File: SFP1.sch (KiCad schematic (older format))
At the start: 20 parts, among them J3 TYCO_1888247-1

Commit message: mark SFP TX_DIS pulldown resistors as 0 Ohm DNF
R84 R105 R185 R187
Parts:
- R105: value R0402_10K_1%_0.0625W_100PPM -> R0402_0R_JUMPER; symbol Resistors_SMD:R0402_10K_1%_0.0625W_100PPM -> Resistors_SMD:R0402_0R_JUMPER; Comment =Value -> 0; ComponentHeight ~~ -> (none); Database Table Name (none) -> Resistors SMD; Footprint Library (none) -> Resistors SMD; Library Name Resistors SMD -> Resistors.DbLib; Library Ref Resistor - 1% -> Resistor; Manufacturer Part Number R0402_10K_1%_0.0625W_100PPM -> R0402_0R_JUMPER; Manufacturer1 Part Number 232270671003L -> 232270591001L; PackageDescription ~~ -> (none); Part Description General Purpose Thick Film Chip Resistor -> 1A (0.05R Max DC Resistance) Zero Ohm Jumper; Part Number R0402_10K_1%_0.0625W_100PPM -> R0402_0R_JUMPER; Power 0.0625W -> (none); Sense Comment ~~ -> (none); Status Comment ~~ -> (none); TC ±100ppm/°C -> (none); Tolerance ±1% -> (none); Val 10k -> 0; Voltage ~~ -> (none); ~ 10k -> DNP
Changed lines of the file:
@@
 $EndComp
 $Comp
-L Resistors_SMD:R0402_10K_1%_0.0625W_100PPM R?
+L Resistors_SMD:R0402_0R_JUMPER R?
 U 1 1 5C64FA82
 P 7750 3850
@@
 AR Path="/5BABAC65/5C64FA82" Ref="R105"  Part="1"
 F 0 "R105" V 7854 3910 50  0000 L CNN
-F 1 "R0402_10K_1%_0.0625W_100PPM" H 7750 3640 60  0001 L CNN
+F 1 "R0402_0R_JUMPER" H 7750 3640 60  0001 L CNN
 F 2 "Marble:RESC1005X40N" H 7750 2830 60  0001 L CNN
 F 3 "\\\\cern.ch\\dfs\\Applications\\Altium\\Datasheets\\R0402_Phycomp_RC0402.pdf" H 7750 3460 60  0001 L CNN
-F 4 "10k" V 7945 3910 50  0000 L CNN "~"
-F 5 "R0402_10K_1%_0.0625W_100PPM" H 7750 3370 60  0001 L CNN "Part Number"
-F 6 "Resistor - 1%" H 7750 3280 60  0001 L CNN "Library Ref"
+F 4 "DNP" V 7945 3910 50  0000 L CNN "~"
+F 5 "R0402_0R_JUMPER" H 7750 3370 60  0001 L CNN "Part Number"
+F 6 "Resistor" H 7750 3280 60  0001 L CNN "Library Ref"
 F 7 "SchLib\\Resistors.SchLib" H 7750 3190 60  0001 L CNN "Library Path"
-F 8 "=Value" H 7750 3100 60  0001 L CNN "Comment"
+F 8 "0" H 7750 3100 60  0001 L CNN "Comment"
 F 9 "Standard" H 7750 3010 60  0001 L CNN "Component Kind"
 F 10 "Standard" H 7750 2920 60  0001 L CNN "Component Type"
-F 11 "~~" H 7750 2740 60  0001 L CNN "PackageDescription"
+F 11 " " H 7750 2740 60  0001 L CNN "PackageDescription"
 F 12 "2" H 7750 2650 60  0001 L CNN "Pin Count"
 F 13 "PcbLib\\Resistors SMD.PcbLib" H 7750 2560 60  0001 L CNN "Footprint Path"
 F 14 "RESC1005X40N" H 7750 2470 60  0001 L CNN "Footprint Ref"
-F 15 "10k" H 7750 2380 60  0001 L CNN "Val"
+F 15 "0" H 7750 2380 60  0001 L CNN "Val"
 F 16 "Not Recommended" H 7750 2290 60  0001 L CNN "Status"
-F 17 "0.0625W" H 7750 2200 60  0001 L CNN "Power"
-F 18 "±100ppm/°C" H 7750 2110 60  0001 L CNN "TC"
-F 19 "~~" H 7750 2020 60  0001 L CNN "Voltage"
-F 20 "±1%" H 7750 1930 60  0001 L CNN "Tolerance"
-F 21 "General Purpose Thick Film Chip Resistor" H 7750 1840 60  0001 L CNN "Part Description"
+F 17 " " H 7750 2200 60  0001 L CNN "Power"
+F 18 " " H 7750 2110 60  0001 L CNN "TC"
+F 19 " " H 7750 2020 60  0001 L CNN "Voltage"
+F 20 " " H 7750 1930 60  0001 L CNN "Tolerance"
+F 21 "1A (0.05R Max DC Resistance) Zero Ohm Jumper" H 7750 1840 60  0001 L CNN "Part Description"
 F 22 "GENERIC" H 7750 1750 60  0001 L CNN "Manufacturer"
-F 23 "R0402_10K_1%_0.0625W_100PPM" H 7750 1660 60  0001 L CNN "Manufacturer Part Number"
+F 23 "R0402_0R_JUMPER" H 7750 1660 60  0001 L CNN "Manufacturer Part Number"
 F 24 "0402" H 7750 1570 60  0001 L CNN "Case"
 F 25 "No" H 7750 1480 60  0001 L CNN "PressFit"
 F 26 "Yes" H 7750 1390 60  0001 L CNN "Mounted"
-F 27 "~~" H 7750 1300 60  0001 L CNN "Sense Comment"
+F 27 " " H 7750 1300 60  0001 L CNN "Sense Comment"
 F 28 "No" H 7750 1210 60  0001 L CNN "Sense"
-F 29 "~~" H 7750 1120 60  0001 L CNN "Status Comment"
+F 29 " " H 7750 1120 60  0001 L CNN "Status Comment"
 F 30 "No" H 7750 1030 60  0001 L CNN "Socket"
 F 31 "Yes" H 7750 940 60  0001 L CNN "SMD"
-F 32 "~~" H 7750 850 60  0001 L CNN "ComponentHeight"
+F 32 " " H 7750 850 60  0001 L CNN "ComponentHeight"
 F 33 "YAGEO PHYCOMP" H 7750 760 60  0001 L CNN "Manufacturer1 Example"
-F 34 "232270671003L" H 7750 670 60  0001 L CNN "Manufacturer1 Part Number"
+F 34 "232270591001L" H 7750 670 60  0001 L CNN "Manufacturer1 Part Number"
 F 35 "0.4mm" H 7750 580 60  0001 L CNN "Manufacturer1 ComponentHeight"
 F 36 "\\\\cern.ch\\dfs\\Applications\\Altium\\Datasheets\\R0402_Phycomp_RC0402.pdf" H 7750 490 60  0001 L CNN "HelpURL"
@@
 F 38 "12/03/07 00:00:00" H 7750 310 60  0001 L CNN "CreateDate"
 F 39 "10/17/12 00:00:00" H 7750 220 60  0001 L CNN "LatestRevisionDate"
-F 40 "Resistors SMD" H 7750 130 60  0001 L CNN "Library Name"
+F 40 "Resistors.DbLib" H 7750 130 60  0001 L CNN "Library Name"
 F 41 "This work is licensed under the Creative Commons CC-BY-SA 4.0 License. To the extent that circuit schematics that use Licensed Material can be considered to be ‘Adapted Material’, then the copyright holder waives article 3.b of the license with respect to these schematics." H 7750 40  60  0001 L CNN "License"
+F 42 "Resistors SMD" H 7750 3850 50  0001 C CNN "Database Table Name"
+F 43 "Resistors SMD" H 7750 3850 50  0001 C CNN "Footprint Library"
 	1    7750 3850
 	0    1    1    0

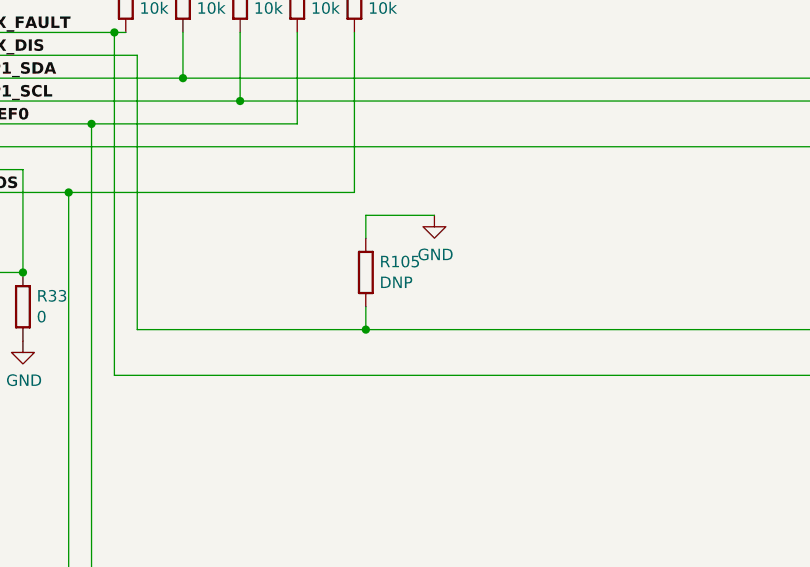
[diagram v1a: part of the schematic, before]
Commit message: Mark R84 R105 R185 R187 dnf in a way that KiBom understands
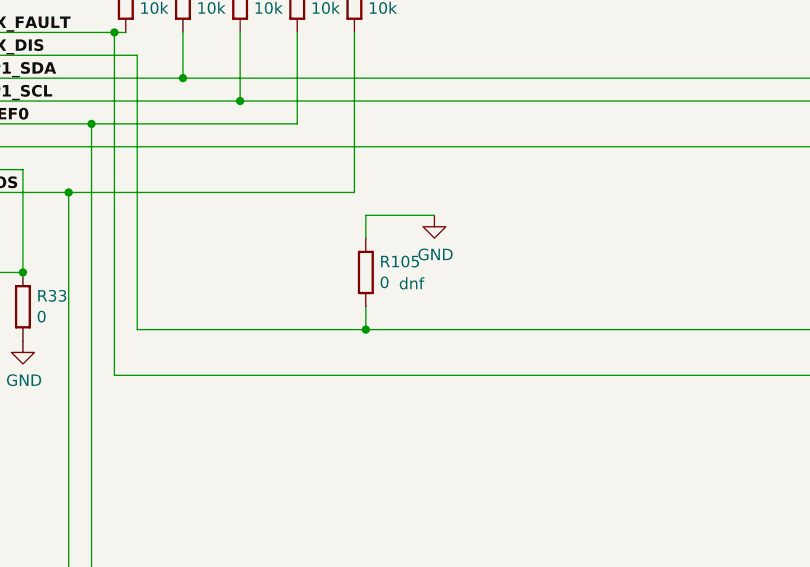
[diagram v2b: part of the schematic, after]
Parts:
- R105: config (none) -> dnf; ~ DNP -> 0
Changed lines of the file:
@@
 F 2 "Marble:RESC1005X40N" H 7750 2830 60  0001 L CNN
 F 3 "\\\\cern.ch\\dfs\\Applications\\Altium\\Datasheets\\R0402_Phycomp_RC0402.pdf" H 7750 3460 60  0001 L CNN
-F 4 "DNP" V 7945 3910 50  0000 L CNN "~"
+F 4 "0" V 7945 3910 50  0000 L CNN "~"
 F 5 "R0402_0R_JUMPER" H 7750 3370 60  0001 L CNN "Part Number"
 F 6 "Resistor" H 7750 3280 60  0001 L CNN "Library Ref"
@@
 F 42 "Resistors SMD" H 7750 3850 50  0001 C CNN "Database Table Name"
 F 43 "Resistors SMD" H 7750 3850 50  0001 C CNN "Footprint Library"
+F 44 "dnf" V 7950 4050 50  0000 C CNN "config"
 	1    7750 3850
 	0    1    1    0

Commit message: Get rid of most .DbLib suffixes in Library Name attributes
Enough that KiBoM no longer complains about them
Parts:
- R105: Library Name Resistors.DbLib -> Resistors SMD
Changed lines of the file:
@@
 F 38 "12/03/07 00:00:00" H 7750 310 60  0001 L CNN "CreateDate"
 F 39 "10/17/12 00:00:00" H 7750 220 60  0001 L CNN "LatestRevisionDate"
-F 40 "Resistors.DbLib" H 7750 130 60  0001 L CNN "Library Name"
+F 40 "Resistors SMD" H 7750 130 60  0001 L CNN "Library Name"
 F 41 "This work is licensed under the Creative Commons CC-BY-SA 4.0 License. To the extent that circuit schematics that use Licensed Material can be considered to be ‘Adapted Material’, then the copyright holder waives article 3.b of the license with respect to these schematics." H 7750 40  60  0001 L CNN "License"
 F 42 "Resistors SMD" H 7750 3850 50  0001 C CNN "Database Table Name"

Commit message: Get rid of more useless inconsistencies in Comment attributes
Makes for quieter KiBoM runs
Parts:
- R105: Comment 0 -> =Value
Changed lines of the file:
@@
 F 6 "Resistor" H 7750 3280 60  0001 L CNN "Library Ref"
 F 7 "SchLib\\Resistors.SchLib" H 7750 3190 60  0001 L CNN "Library Path"
-F 8 "0" H 7750 3100 60  0001 L CNN "Comment"
+F 8 "=Value" H 7750 3100 60  0001 L CNN "Comment"
 F 9 "Standard" H 7750 3010 60  0001 L CNN "Component Kind"
 F 10 "Standard" H 7750 2920 60  0001 L CNN "Component Type"

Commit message: Get rid of "~" attribute in instances
This makes instances line up better with our library
Use a very short python program to rename "~" to "Val" and remove the old "Val".
Required a little pre-patch to correctly handle R297 R298 R299 R300 R162 R274 R197 R198, which had no "~" field.
No net changes to "Val" field contents.
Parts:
- C28, C32, C34, C35: ~ 100nF -> (none)
- C29, C31: ~ 1uF -> (none)
- C30, C33: ~ 10uF -> (none)
- Cage1, J3: Val (none) -> SFP+; ~ SFP+ -> (none)
- L1, L2: ~ 120R@100MHz -> (none)
- R105, R33: ~ 0 -> (none)
- R32, R34, R35, R36, R37, R38: ~ 10k -> (none)
